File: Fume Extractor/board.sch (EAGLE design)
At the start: 12 parts, among them IC1 MCP73831/OT, IC2 DW01, J1 AMP FCI 10103594-0001LF, T1 DMN3024LSD, U1 1048

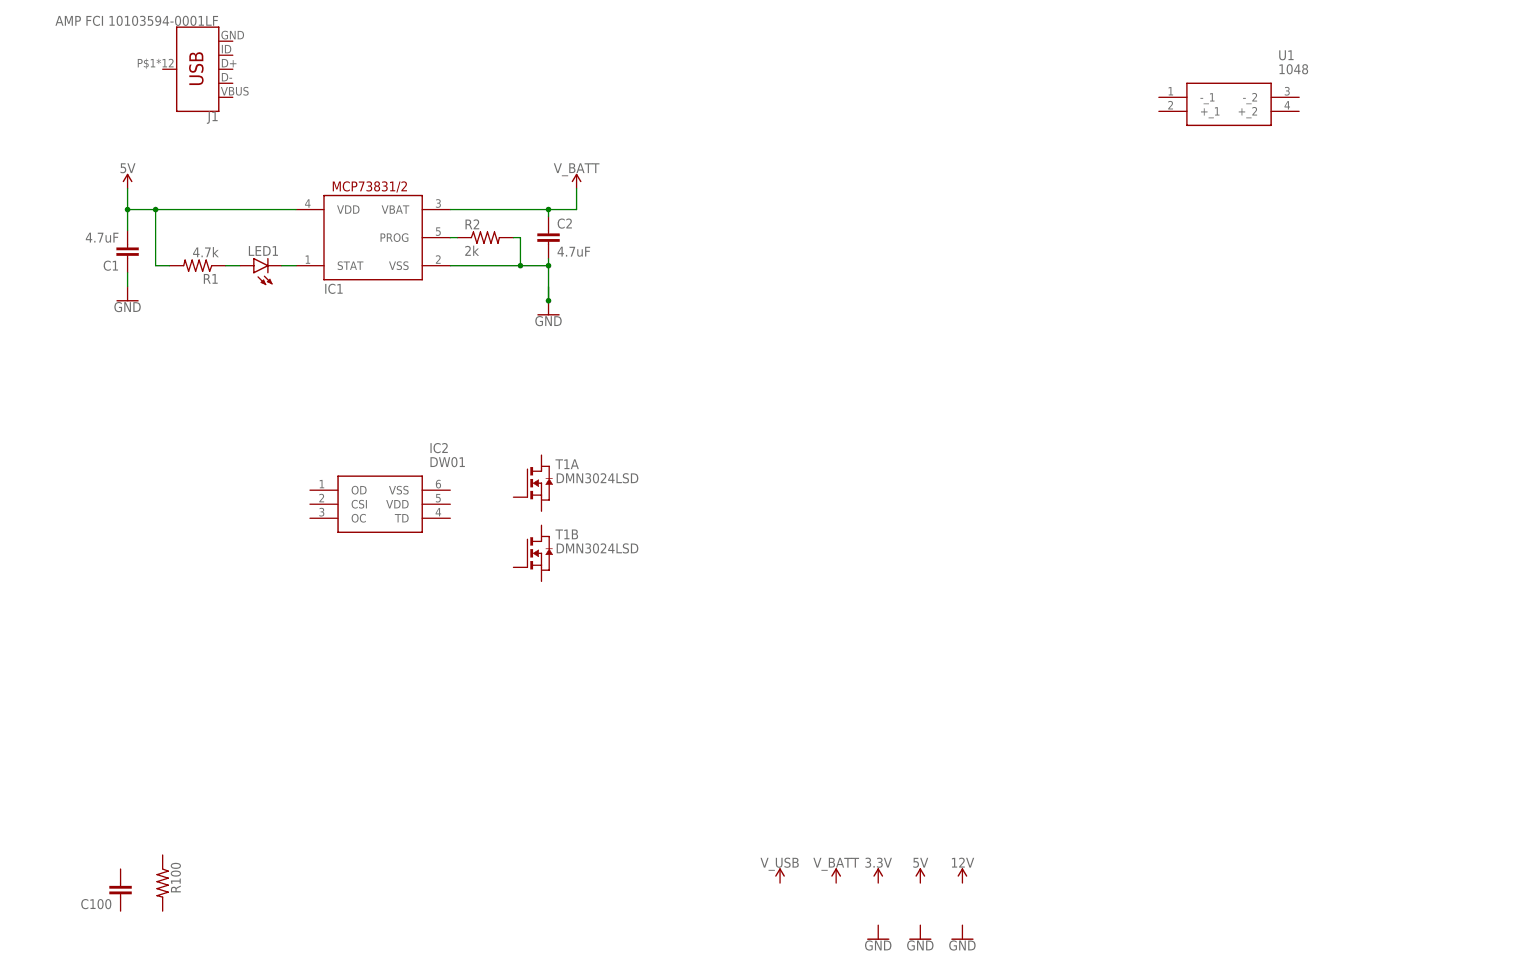
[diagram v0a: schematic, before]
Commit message: battery charging + protection circuit
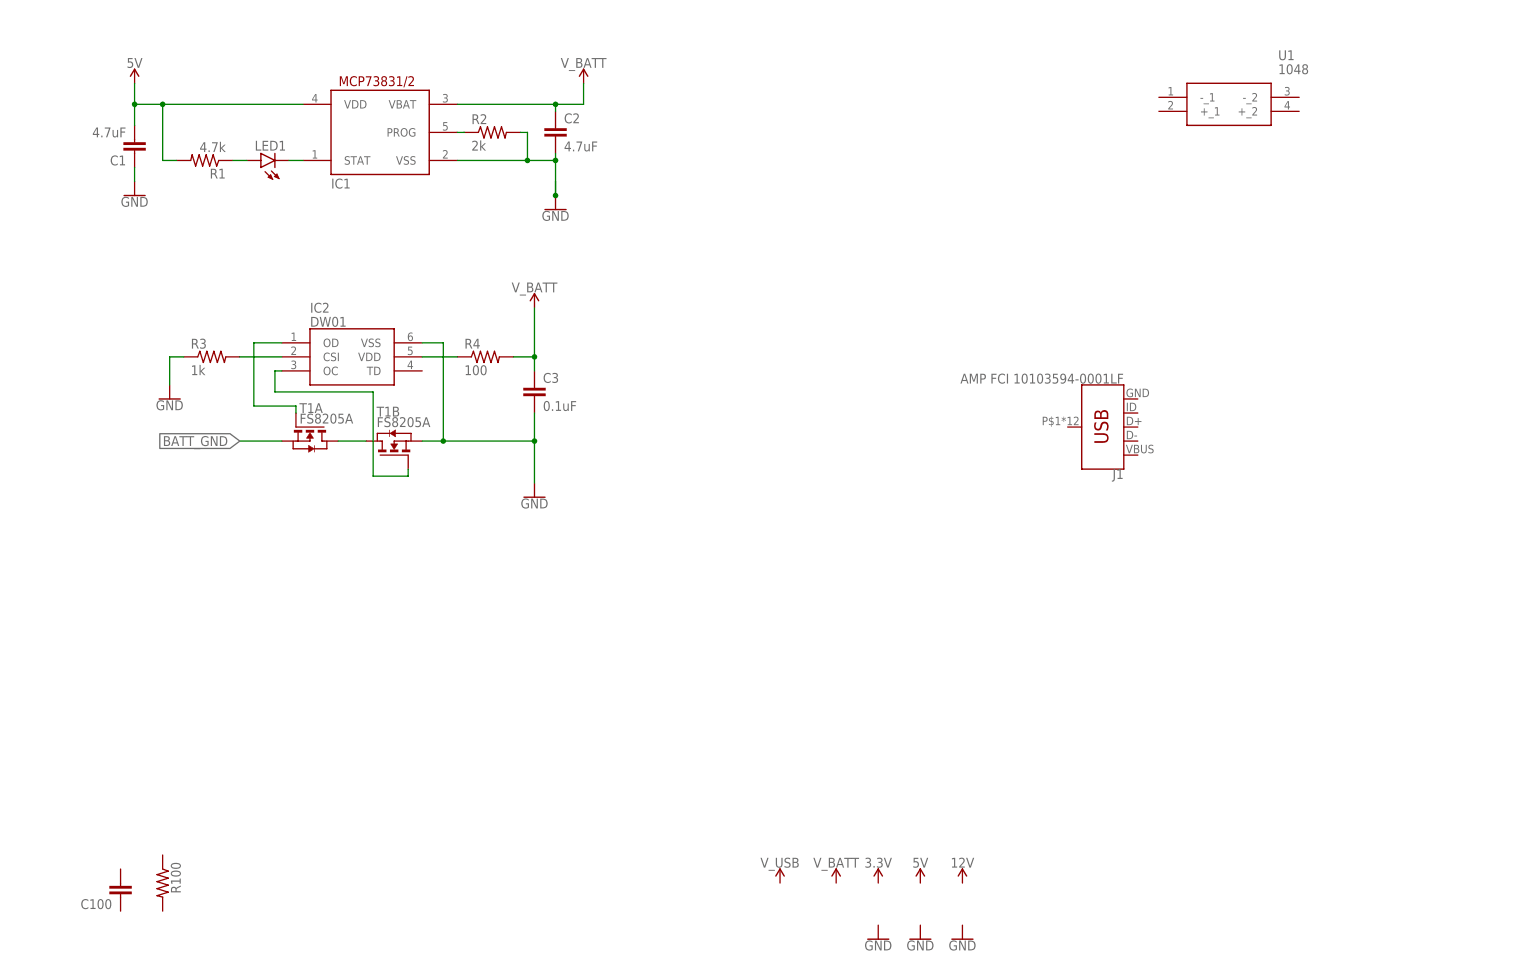
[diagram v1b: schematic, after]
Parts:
- added C3: 0.1uF, rcl:C-EUC0805
- added R3: 1k, rcl:R-US_R0805
- added R4: 100, rcl:R-US_R0805
- T1: value DMN3024LSD -> FS8205A; device FS8205A:DMN3024LSD -> FS8205A:FS8205A-MOSFET
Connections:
- new net BATT_GND: T1A.S
- new net N$10: IC2.OC, T1B.G
- new net N$4: T1A.D, T1B.D
- new net N$5: IC2.CSI, R3.2
- new net N$6: IC2.OD, T1A.G
- new net N$7: IC2.VDD, R4.1
- net GND: now also C3.2, IC2.VSS, R3.1, T1B.S
- net V_BATT: now also C3.1, R4.2
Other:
- moved on the sheet: C1, C2, IC1, IC2, J1, LED1, R1, R2, T1A, T1B

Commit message: MCP72831 circuit backup, TP4056
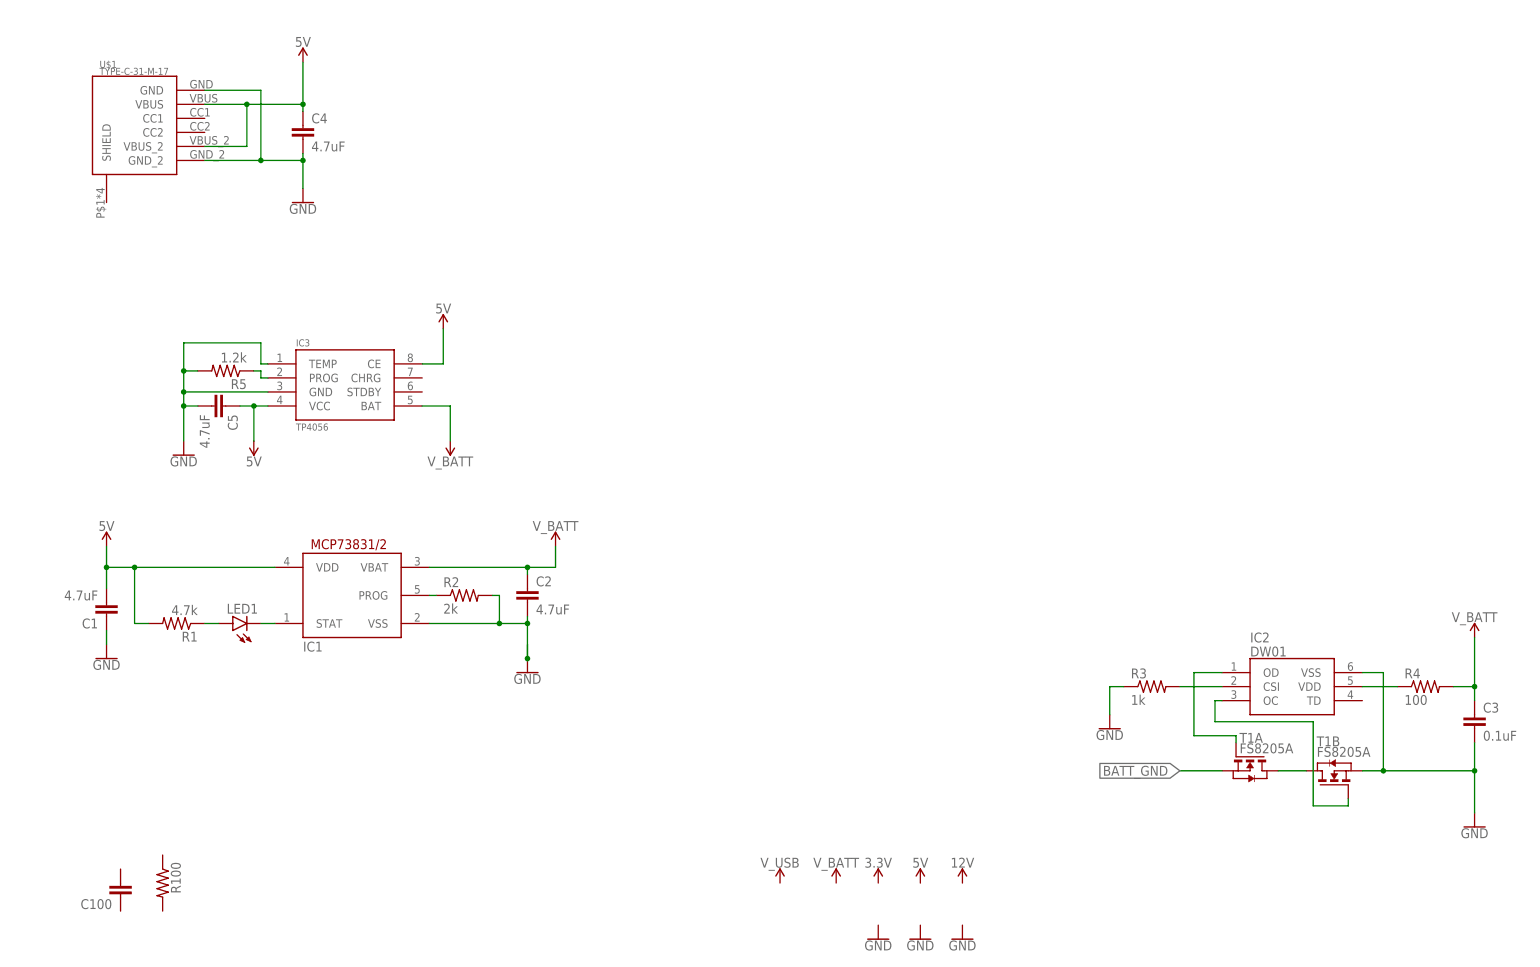
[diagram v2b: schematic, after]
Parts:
- removed J1: AMP FCI 10103594-0001LF, SparkFun-Connectors:USB_MICRO-B_HALF_PTH
- removed U1: 1048, SamacSys_Parts:1048
- added C4, C5: 4.7uF, rcl:C-EUC0805
- added IC3: TP4056, TP4056:TP4056
- added R5: 1.2k, rcl:R-US_R0805
- added U$1: TYPE-C-31-M-17, Type-C_Hroparts:TYPE-C-31-M-17
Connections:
- new net N$8: IC3.PROG, R5.1
- net 5V: now also C4.1, C5.1, IC3.CE, IC3.VCC, U$1.VBUS, U$1.VBUS_2
- net GND: now also C4.2, C5.2, IC3.GND, IC3.TEMP, R5.2, U$1.GND, U$1.GND_2
- net V_BATT: now also IC3.BAT
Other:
- moved on the sheet: C1, C2, C3, IC1, IC2, LED1, R1, R2, R3, R4, T1A, T1B

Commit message: TP4056 + DW01 + Type C input
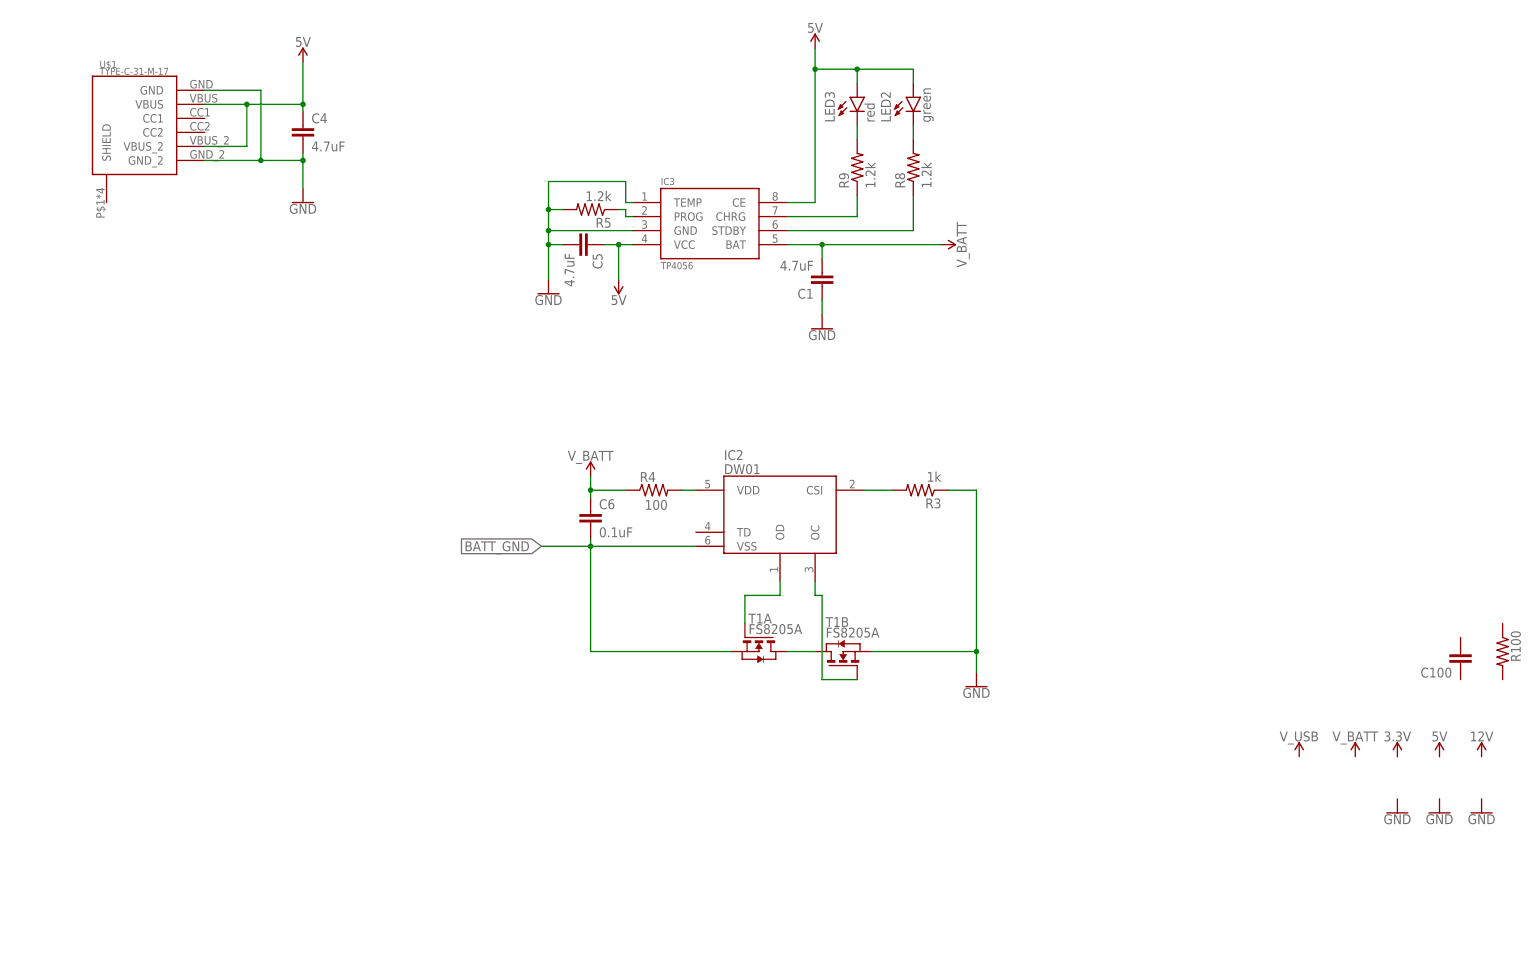
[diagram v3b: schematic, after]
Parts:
- removed C2: 4.7uF, rcl:C-EUC0805
- removed C3: 0.1uF, rcl:C-EUC0805
- removed IC1: MCP73831/OT, adafruit:MCP73831/OT
- removed LED1: (no value), led:LEDCHIP-LED0805
- removed R1: 4.7k, rcl:R-US_R0805
- removed R2: 2k, rcl:R-US_R0805
- added C6: 0.1uF, rcl:C-EUC0805
- added LED2: green, led:LEDCHIP-LED0805
- added LED3: red, led:LEDCHIP-LED0805
- added R8, R9: 1.2k, rcl:R-US_R0805
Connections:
- removed net N$7 (its old number): IC2.VDD, R4.1
- new net N$11: LED3.C, R9.2
- new net N$9: LED2.C, R8.2
- net 5V: now also LED2.A, LED3.A; no longer C1.2, IC1.VDD, R1.2
- net BATT_GND: now also C6.2, IC2.VSS
- net GND: no longer C2.2, C3.2, IC1.VSS, IC2.VSS, R2.2
- net N$1: now also IC2.VDD, R4.2; no longer LED1.A, R1.1
- net N$2: now also IC3.CHRG, R9.1; no longer IC1.STAT, LED1.C
- net N$3: now also IC3.STDBY, R8.1; no longer IC1.PROG, R2.1
- net V_BATT: now also C1.2, C6.1, R4.1; no longer C2.1, C3.1, IC1.VBAT, R4.2
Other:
- moved on the sheet: C1, C100, C5, IC2, IC3, R100, R3, R4, R5, T1A, T1B
